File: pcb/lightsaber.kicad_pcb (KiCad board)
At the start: 2 copper layers, 107.6 x 27.9 mm, 49 parts, among them J1 2012670005, J2 ESP32 Prog, J3 ESP32 JTAG, J4 Screw_Terminal_01x05, Q1 PMOS, SW1 SW_Push, SW2 SW_Push, U1 ME6211A33PG-N, U2 ESP32-S3-WROOM-1, U3 BQ21040DBVR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

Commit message: Adding multiverse
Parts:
- added D5: 1N4148, Diode_SMD:D_SOD-323, F.Cu at (142.2, 70.7)
- added Q2: NPN, Package_TO_SOT_SMD:SOT-23, F.Cu at (147.1, 74.7)
- added R11: 1k, Resistor_SMD:R_0603_1608Metric, F.Cu at (142.6, 73.7)
- added R12: 10k, Resistor_SMD:R_0603_1608Metric, F.Cu at (142.6, 76.2)
- added R13: 10R, Resistor_SMD:R_0402_1005Metric, F.Cu at (146.1, 77.9)
- moved R8 27.1 mm to (168.6, 84.5), turned to 90 degrees
- moved R9 23.7 mm to (162.3, 91.1), turned to 180 degrees
- moved C16 10.9 mm to (195.6, 101.5)
- moved C17 10.6 mm to (195.9, 88.5)
- moved R1 4.24 mm to (179.2, 82.9), turned to 0 degrees
- moved U5 3.62 mm to (156.8, 99.1)
- moved C20 2.34 mm to (156.8, 96.7)
- moved C8 1.99 mm to (182.2, 82.9), turned to 0 degrees
- moved C10 1.67 mm to (177.8, 84.3), turned to 0 degrees
- moved C9 1.13 mm to (182.1, 84.3), turned to 180 degrees

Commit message: Initial routing
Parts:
- removed C20: 100nF, Capacitor_SMD:C_0402_1005Metric
- removed JP1, JP2: SolderJumper_2_Open, Jumper:SolderJumper-2_P1.3mm_Open_Pad1.0x1.5mm
- removed U5: AHT20, AHT20:PSON100P300X300X110-6N
- added C21: 1uF, Capacitor_SMD:C_0402_1005Metric, F.Cu at (195.8, 84.6)
- added U6: 5994, CityTheatrical:Module 5994, F.Cu at (186.6, 96.0)
- moved J2 101.3 mm to (124.5, 107.3)
- moved J3 98.2 mm to (126.3, 85.3), turned to 180 degrees
- moved D5 89.3 mm to (230.5, 84.2)
- moved Q2 89.3 mm to (235.4, 88.2)
- moved R11 89.3 mm to (230.9, 87.2)
- moved R12 89.3 mm to (230.9, 89.7)
- moved R13 89.3 mm to (234.4, 91.4)
- moved C8 35.2 mm to (157.9, 108.3), turned to 180 degrees
- moved C9 33.1 mm to (158.0, 106.9), turned to 0 degrees
- moved R1 31.3 mm to (160.9, 108.3), turned to 180 degrees
- moved C10 27.4 mm to (162.3, 106.9), turned to 180 degrees
- moved R8 23.9 mm to (176.7, 107.0), turned to -90 degrees
- moved R9 21.8 mm to (177.7, 106.6), turned to -90 degrees
- moved C17 18.2 mm to (207.4, 102.6)
- moved SW2 18.1 mm to (212.5, 102.6)
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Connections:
- U2 pad 10: unconnected-(U2-GPIO17/U1TXD/ADC2_CH6-Pad10) -> CTI_nRESET
- U2 pad 11: unconnected-(U2-GPIO18/U1RXD/ADC2_CH7/CLK_OUT3-Pad11) -> CTI_I2C_nATTN
- U2 pad 13: Net-(JP2-A) -> D-
- U2 pad 14: Net-(JP1-A) -> D+
- U2 pad 18: unconnected-(U2-GPIO10/TOUCH10/ADC1_CH9/FSPICS0/FSPIIO4/SUBSPICS0-Pad18) -> CTI_SPI_nSS
- U2 pad 19: unconnected-(U2-GPIO11/TOUCH11/ADC2_CH0/FSPID/FSPIIO5/SUBSPID-Pad19) -> CTI_SPI_MOSI
- U2 pad 20: unconnected-(U2-GPIO12/TOUCH12/ADC2_CH1/FSPICLK/FSPIIO6/SUBSPICLK-Pad20) -> CTI_SPI_CLK
- U2 pad 21: unconnected-(U2-GPIO13/TOUCH13/ADC2_CH2/FSPIQ/FSPIIO7/SUBSPIQ-Pad21) -> CTI_SPI_MISO
- U2 pad 22: unconnected-(U2-GPIO14/TOUCH14/ADC2_CH3/FSPIWP/FSPIDQS/SUBSPIWP-Pad22) -> CTI_SPI_nATTN
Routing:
- net ESP_EN: track 0.00 -> 64.1 mm
- net GND: track 25.9 -> 68.4 mm, vias 9 -> 31
- net CTI_SPI_nATTN: track 0.00 -> 23.7 mm
- net CTI_SPI_CLK: track 0.00 -> 21.2 mm
- net CTI_SPI_MISO: track 0.00 -> 20.4 mm, vias 0 -> 2
- net CTI_I2C_nATTN: track 0.00 -> 19.3 mm, vias 0 -> 2
- net CTI_SPI_MOSI: track 0.00 -> 17.7 mm
- net +3.3V: track 4.98 -> 22.4 mm, vias 0 -> 4
- net CTI_SPI_nSS: track 0.00 -> 15.6 mm
- net ESP_IO0: track 0.00 -> 9.03 mm
- net +BATT: track 0.00 -> 6.29 mm
- net ESP_USER_BUTTON: track 0.00 -> 1.16 mm
- net ESP32_I2C_SDA: track 0.00 -> 0.87 mm
- added copper zone on In2.Cu, net +3.3V
- added copper zone on F.Cu, net GND
- added copper zone on In1.Cu, net GND
- removed copper zone on B.Cu, net GND
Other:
- board size 107.6 x 27.9 mm -> 120 x 27.9 mm
- copper layers 2 -> 4

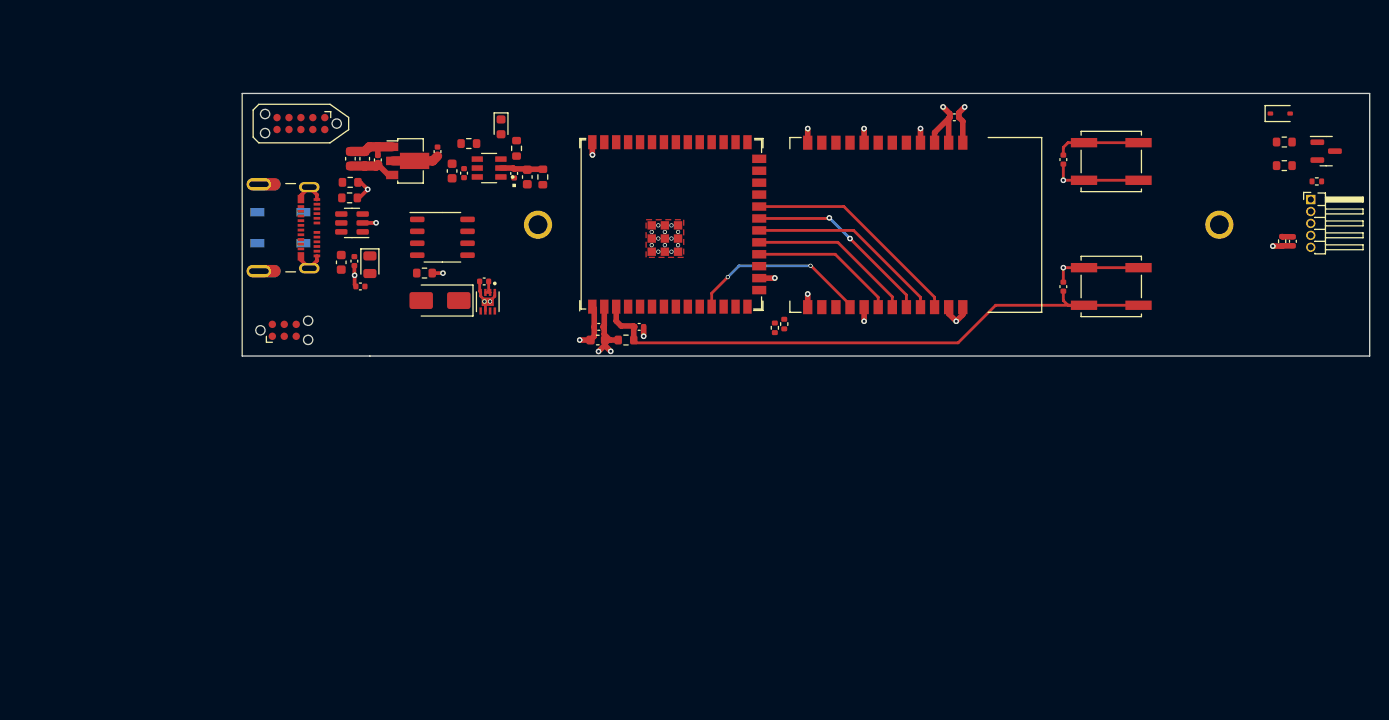
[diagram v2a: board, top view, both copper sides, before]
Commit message: Fuses and current detection
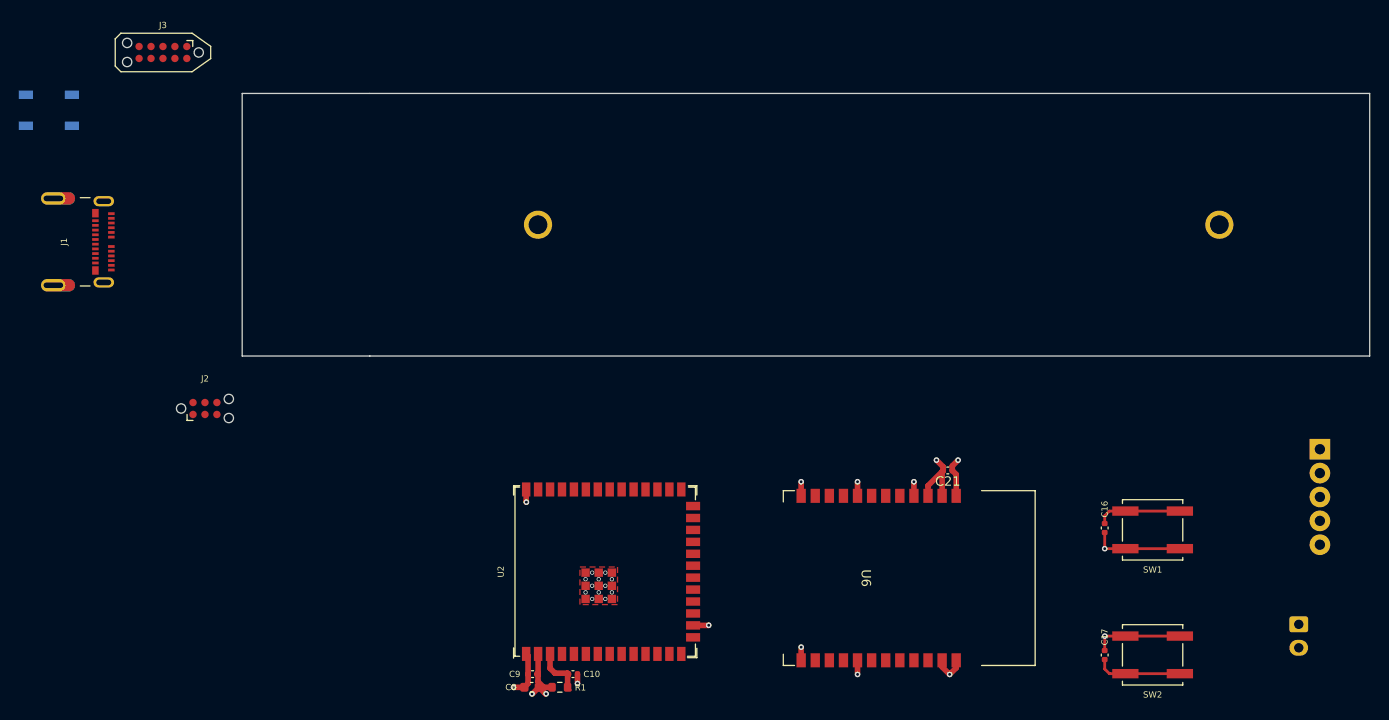
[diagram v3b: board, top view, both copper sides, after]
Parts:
- removed C1, C12, C15, C6, C7: 10uF, Capacitor_SMD:C_0603_1608Metric
- removed C13, C14, C19, C2, C4, C5: 1uF, Capacitor_SMD:C_0402_1005Metric
- removed C18, C3: 100nF, Capacitor_SMD:C_0402_1005Metric
- removed D1: Schottky, Diode_SMD:D_SMA
- removed D2: SP0505BAHT, Package_TO_SOT_SMD:SOT-23-6
- removed D3: LED, LED_SMD:LED_0603_1608Metric
- removed D5: 1N4148, Diode_SMD:D_SOD-323
- removed FB1: FerriteBead, Diode_SMD:D_0805_2012Metric
- removed Q1: PMOS, Package_SO:SSOP-8_3.9x5.05mm_P1.27mm
- removed Q2: NPN, Package_TO_SOT_SMD:SOT-23
- removed R10: 10k, Resistor_SMD:R_0402_1005Metric
- removed R11, R6, R7: 1k, Resistor_SMD:R_0603_1608Metric
- removed R12, R5: 10k, Resistor_SMD:R_0603_1608Metric
- removed R13: 10R, Resistor_SMD:R_0402_1005Metric
- removed R2, R3: 5.1k, Resistor_SMD:R_0603_1608Metric
- removed R4: 100k, Resistor_SMD:R_0603_1608Metric
- removed R8, R9: 4.7k, Resistor_SMD:R_0402_1005Metric
- removed U1: ME6211A33PG-N, Package_TO_SOT_SMD:SOT-89-3
- removed U3: BQ21040DBVR, BQ21040DBVR:SOT95P280X145-6N
- removed U4: MAX17048G+T10, MAX17048G_T10:SON50P200X200X80-9N
- added J5: Conn_01x02, Connector_JST:JST_XH_S2B-XH-A-1_1x02_P2.50mm_Horizontal, B.Cu at (232.4, 138.6)
- J4: footprint Connector_PinHeader_1.27mm:PinHeader_1x05_P1.27mm_Horizontal -> TerminalBlock_Phoenix:TerminalBlock_Phoenix_MPT-0,5-5-2.54_1x05_P2.54mm_Horizontal; moved to B.Cu
- moved C16 39.4 mm to (211.8, 128.3)
- moved SW2 39.4 mm to (216.9, 141.8)
- moved SW1 39.4 mm to (216.9, 128.5)
- moved C17 39.4 mm to (211.8, 141.8)
- moved C8 37.6 mm to (150.8, 145.2)
- moved R1 37.6 mm to (153.8, 145.2)
- moved C10 37.6 mm to (155.2, 143.8)
- moved C9 37.6 mm to (150.9, 143.8)
- moved U2 37.6 mm to (158.5, 132.9)
- moved C21 37.6 mm to (195.1, 122.2)
- moved U6 37.6 mm to (185.9, 133.6)
- moved D4 27.6 mm to (99.5, 83.8)
- moved J4 26.6 mm to (234.7, 119.9), turned to -90 degrees
- moved J1 21.9 mm to (105.3, 97.8)
- moved J3 16.5 mm to (111.6, 77.7)
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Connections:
- C11 pad 1: +BATT -> Net-(C11-VBAT)
- J4 pad 1: +BATT -> LED_PWR
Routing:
- net ESP_EN: track 64.1 -> 14.8 mm
- net GND: track 68.4 -> 43.5 mm, vias 31 -> 25
- net CTI_SPI_nATTN: track 23.7 -> 0.00 mm
- net CTI_SPI_CLK: track 21.2 -> 0.00 mm
- net CTI_SPI_MISO: track 20.4 -> 0.00 mm, vias 2 -> 0
- net CTI_I2C_nATTN: track 19.3 -> 0.25 mm, vias 2 -> 0
- net CTI_SPI_MOSI: track 17.7 -> 0.00 mm
- net CTI_SPI_nSS: track 15.6 -> 0.00 mm
- net +3.3V: track 22.4 -> 14.4 mm, vias 4 -> 3
- net +BATT: track 6.29 -> 0.00 mm
- net VCC: track 4.95 -> 0.00 mm
- net ESP_USER_BUTTON: track 1.16 -> 0.00 mm
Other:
- board text removed: "."

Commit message: General tidyup
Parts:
- added C1: 10uF, Capacitor_SMD:C_0603_1608Metric, F.Cu at (175.1, 36.1)
- added C12: 10uF, Capacitor_SMD:C_0603_1608Metric, F.Cu at (175.1, 41.1)
- added C13: 1uF, Capacitor_SMD:C_0402_1005Metric, F.Cu at (177.4, 45.9)
- added C14: 1uF, Capacitor_SMD:C_0402_1005Metric, F.Cu at (177.4, 47.9)
- added C15: 10uF, Capacitor_SMD:C_0603_1608Metric, F.Cu at (175.1, 43.7)
- added C18: 100nF, Capacitor_SMD:C_0402_1005Metric, F.Cu at (177.4, 49.8)
- added C19: 1uF, Capacitor_SMD:C_0402_1005Metric, F.Cu at (177.4, 51.8)
- added C2: 1uF, Capacitor_SMD:C_0402_1005Metric, F.Cu at (174.5, 45.9)
- added C22: 100nF, Capacitor_SMD:C_0402_1005Metric, F.Cu at (180.2, 45.9)
- added C23: 100nF, Capacitor_SMD:C_0402_1005Metric, F.Cu at (180.2, 47.9)
- added C24: 100nF, Capacitor_SMD:C_0402_1005Metric, F.Cu at (180.2, 49.8)
- added C25: 1nF, Capacitor_SMD:C_0402_1005Metric, F.Cu at (180.2, 51.8)
- added C3: 100nF, Capacitor_SMD:C_0402_1005Metric, F.Cu at (174.5, 47.9)
- added C4: 1uF, Capacitor_SMD:C_0402_1005Metric, F.Cu at (174.5, 49.8)
- added C5: 1uF, Capacitor_SMD:C_0402_1005Metric, F.Cu at (174.5, 51.8)
- added C6: 10uF, Capacitor_SMD:C_0603_1608Metric, F.Cu at (175.1, 38.6)
- added D1: Schottky, Diode_SMD:D_SMA, F.Cu at (191.9, 53.8)
- added D2: SP0505BAHT, Package_TO_SOT_SMD:SOT-23-6, F.Cu at (194.6, 58.3)
- added D3: LED, LED_SMD:LED_0603_1608Metric, F.Cu at (194.1, 61.8)
- added D5: 1N4148, Diode_SMD:D_SOD-323, F.Cu at (199.3, 60.6)
- added D6: WS2812B, LED_SMD:LED_WS2812B_PLCC4_5.0x5.0mm_P3.2mm, F.Cu at (185.9, 48.2)
- added F1: 8A Fuse, Littelfuse:0154008DR, F.Cu at (192.0, 38.9)
- added FB1: FerriteBead, Diode_SMD:D_0805_2012Metric, F.Cu at (199.4, 57.6)
- added IC1: BMI055, BMI:QFN50P300X450X100-16N, F.Cu at (189.6, 60.1)
- added Q1: PMOS, Package_SO:SSOP-8_3.9x5.05mm_P1.27mm, F.Cu at (177.3, 56.1)
- added Q2: NPN, Package_TO_SOT_SMD:SOT-23, F.Cu at (184.1, 59.8)
- added R10: 10k, Resistor_SMD:R_0402_1005Metric, F.Cu at (200.3, 39.9)
- added R11: 1k, Resistor_SMD:R_0603_1608Metric, F.Cu at (183.1, 41.1)
- added R12: 10k, Resistor_SMD:R_0603_1608Metric, F.Cu at (183.1, 43.7)
- added R13: 10R, Resistor_SMD:R_0402_1005Metric, F.Cu at (200.3, 41.8)
- added R2: 5.1k, Resistor_SMD:R_0603_1608Metric, F.Cu at (179.1, 36.1)
- added R3: 5.1k, Resistor_SMD:R_0603_1608Metric, F.Cu at (179.1, 38.6)
- added R4: 100k, Resistor_SMD:R_0603_1608Metric, F.Cu at (179.1, 41.1)
- added R5: 10k, Resistor_SMD:R_0603_1608Metric, F.Cu at (179.1, 43.7)
- added R6: 1k, Resistor_SMD:R_0603_1608Metric, F.Cu at (183.1, 36.1)
- added R7: 1k, Resistor_SMD:R_0603_1608Metric, F.Cu at (183.1, 38.6)
- added R8: 4.7k, Resistor_SMD:R_0402_1005Metric, F.Cu at (200.3, 35.9)
- added R9: 4.7k, Resistor_SMD:R_0402_1005Metric, F.Cu at (200.3, 37.9)
- added U1: ME6211A33PG-N, Package_TO_SOT_SMD:SOT-89-3, F.Cu at (185.1, 54.6)
- added U3: BQ21040DBVR, BQ21040:SOT95P280X145-6N, F.Cu at (199.1, 53.8)
- added U4: MAX17048G+T10, MAX17048:SON50P200X200X80-9N, F.Cu at (175.7, 61.2)
- added U7: ACS725xLCTR-10AU, Package_SO:SOIC-8_3.9x4.9mm_P1.27mm, F.Cu at (194.3, 48.1)
- moved U2 5.41 mm to (163.9, 133.5)
- moved C10 5.37 mm to (160.6, 144.4)
- moved C8 5.37 mm to (156.2, 145.8)
- moved C9 5.37 mm to (156.3, 144.4)
- moved R1 5.37 mm to (159.2, 145.8)
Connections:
- D4 pad 2: unconnected-(D4-DOUT-Pad2) -> Net-(D4-DOUT)
- U2 pad 15: unconnected-(U2-GPIO3/TOUCH3/ADC1_CH2-Pad15) -> ESP_CURRENT_SENSE
- U2 pad 4: unconnected-(U2-GPIO4/TOUCH4/ADC1_CH3-Pad4) -> ESP32_BMI_GYRO_1
- U2 pad 5: unconnected-(U2-GPIO5/TOUCH5/ADC1_CH4-Pad5) -> ESP32_BMI_GYRO_2
- U2 pad 6: unconnected-(U2-GPIO6/TOUCH6/ADC1_CH5-Pad6) -> ESP32_BMI_ACCEL_1
- U2 pad 7: unconnected-(U2-GPIO7/TOUCH7/ADC1_CH6-Pad7) -> ESP32_BMI_ACCEL_2

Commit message: ERC Complete
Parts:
- removed C1, C12, C15, C6, C8: 10uF, Capacitor_SMD:C_0603_1608Metric
- removed C10, C13, C14, C16, C17, C19, C2, C21, C4, C5, C9: 1uF, Capacitor_SMD:C_0402_1005Metric
- removed C18, C22, C23, C24, C3: 100nF, Capacitor_SMD:C_0402_1005Metric
- removed C25: 1nF, Capacitor_SMD:C_0402_1005Metric
- removed D1: Schottky, Diode_SMD:D_SMA
- removed D2: SP0505BAHT, Package_TO_SOT_SMD:SOT-23-6
- removed D3: LED, LED_SMD:LED_0603_1608Metric
- removed D4, D6: WS2812B, LED_SMD:LED_WS2812B_PLCC4_5.0x5.0mm_P3.2mm
- removed D5: 1N4148, Diode_SMD:D_SOD-323
- removed F1: 8A Fuse, Littelfuse:0154008DR
- removed FB1: FerriteBead, Diode_SMD:D_0805_2012Metric
- removed IC1: BMI055, BMI:QFN50P300X450X100-16N
- removed J1: 2012670005, Molex:MOLEX_2012670005
- removed J2: ESP32 Prog, Connector:Tag-Connect_TC2030-IDC-NL_2x03_P1.27mm_Vertical
- removed J3: ESP32 JTAG, Connector:Tag-Connect_TC2050-IDC-NL_2x05_P1.27mm_Vertical_with_bottom_clip
- removed J4: Screw_Terminal_01x05, TerminalBlock_Phoenix:TerminalBlock_Phoenix_MPT-0,5-5-2.54_1x05_P2.54mm_Horizontal
- removed J5: Conn_01x02, Connector_JST:JST_XH_S2B-XH-A-1_1x02_P2.50mm_Horizontal
- removed Q1: PMOS, Package_SO:SSOP-8_3.9x5.05mm_P1.27mm
- removed Q2: NPN, Package_TO_SOT_SMD:SOT-23
- removed R1, R12, R5: 10k, Resistor_SMD:R_0603_1608Metric
- removed R10: 10k, Resistor_SMD:R_0402_1005Metric
- removed R11, R6, R7: 1k, Resistor_SMD:R_0603_1608Metric
- removed R13: 10R, Resistor_SMD:R_0402_1005Metric
- removed R2, R3: 5.1k, Resistor_SMD:R_0603_1608Metric
- removed R4: 100k, Resistor_SMD:R_0603_1608Metric
- removed R8, R9: 4.7k, Resistor_SMD:R_0402_1005Metric
- removed SW1, SW2: SW_Push, Button_Switch_SMD:SW_Push_1P1T_NO_CK_KSC6xxJ
- removed U1: ME6211A33PG-N, Package_TO_SOT_SMD:SOT-89-3
- removed U2: ESP32-S3-WROOM-1, Espressif:ESP32-S3-WROOM-1U
- removed U3: BQ21040DBVR, BQ21040:SOT95P280X145-6N
- removed U4: MAX17048G+T10, MAX17048:SON50P200X200X80-9N
- removed U6: 5994, CityTheatrical:Module 5994
- removed U7: ACS725xLCTR-10AU, Package_SO:SOIC-8_3.9x4.9mm_P1.27mm
- moved C11 9.56 mm to (223.5, 95.0)
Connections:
- C11 pad 1: Net-(C11-VBAT) -> +BATT
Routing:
- net GND: track 43.5 -> 0.00 mm, vias 25 -> 0
- net ESP_EN: track 14.8 -> 0.00 mm
- net +3.3V: track 14.4 -> 0.00 mm, vias 3 -> 0
- net ESP_IO0: track 9.03 -> 0.00 mm
- net ESP32_I2C_SDA: track 0.73 -> 0.00 mm
- added copper zone on B.Cu, net GND
- removed copper zone on In2.Cu, net +3.3V
- removed copper zone on F.Cu, net GND
- removed copper zone on In1.Cu, net GND
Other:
- board size 120 x 27.9 mm -> 107.6 x 27.9 mm
- copper layers 4 -> 2
